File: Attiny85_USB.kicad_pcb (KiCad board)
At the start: 2 copper layers, 40.1 x 12.4 mm, 12 parts, among them J1 Conn_01x04, J2 Conn_01x04, U1 ATtiny85-20M

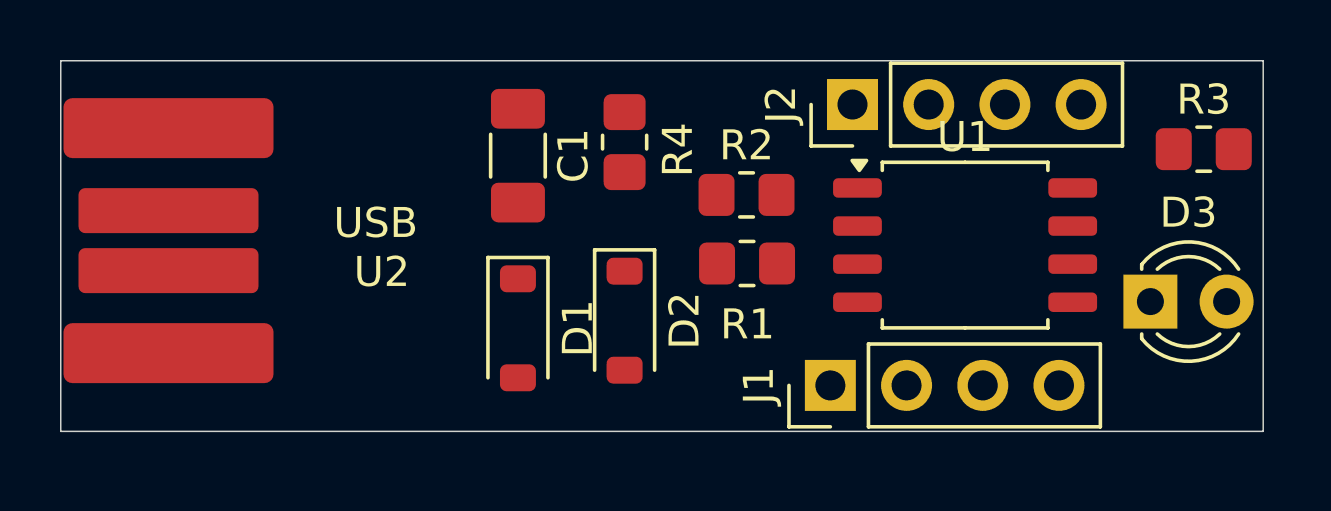
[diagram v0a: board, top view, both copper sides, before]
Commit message: fixing some bugs on the printfoot of the ATtiny85
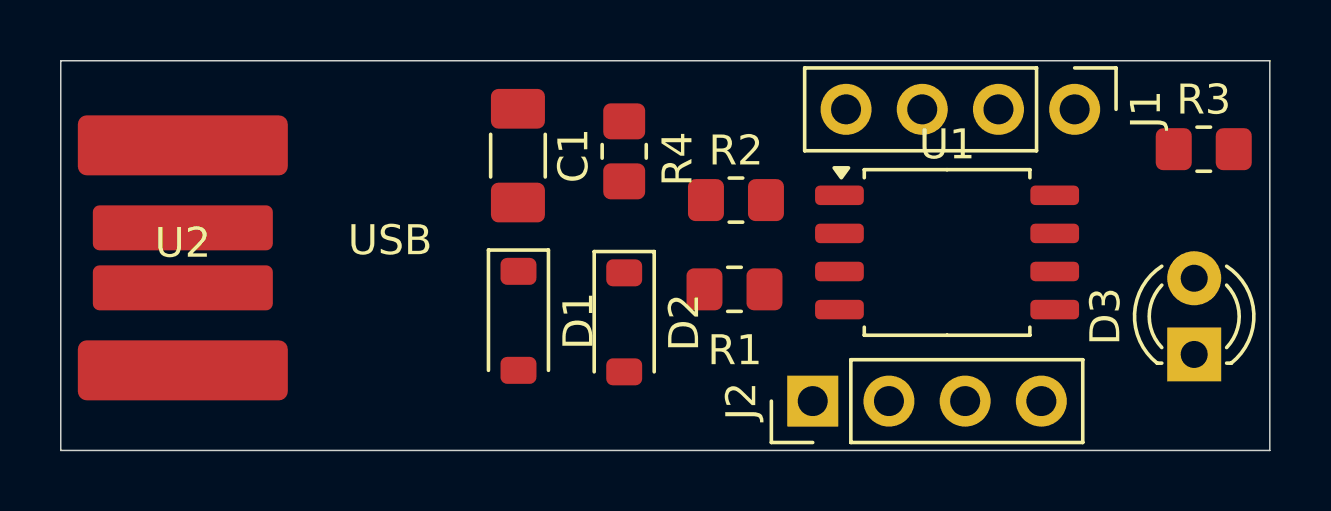
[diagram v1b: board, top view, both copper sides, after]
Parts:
- moved J1 12.3 mm to (139.7, 102.0), turned to -90 degrees
- moved J2 9.97 mm to (131.0, 111.8)
- moved D3 2.29 mm to (143.7, 110.2), turned to 90 degrees
- moved R1 0.96 mm to (128.4, 108.0)
- moved U2 0.75 mm to (110.0, 107.0)
- moved U1 0.65 mm to (135.5, 106.8)
- moved R2 0.39 mm to (128.4, 105.1)
- moved R4 0.31 mm to (124.7, 103.5)
- moved D1 0.25 mm to (121.2, 109.1)
- moved D2 0.06 mm to (124.7, 109.2)
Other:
- board size 40.1 x 12.4 mm -> 40.3 x 13 mm

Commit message: last commit
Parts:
- removed U1: ATtiny85-20M, Package_SO:SOIC-8_5.3x5.3mm_P1.27mm
- added U3: ATtiny85-20S, Package_SO:SOIC-8_5.3x5.3mm_P1.27mm, F.Cu at (135.4, 107.0)
- moved J2 1.07 mm to (132.1, 111.7)
- moved R1 0.58 mm to (128.4, 107.5), turned to 180 degrees
- moved R4 0.48 mm to (124.8, 103.0), turned to -90 degrees
- moved U2 0.40 mm to (109.6, 106.9)
- moved J1 0.25 mm to (139.7, 102.3)
- turned R2 to 180 degrees
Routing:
- net +5V: track 0.00 -> 46.1 mm, vias 0 -> 2
- net GND: track 0.00 -> 37.5 mm
- net Net-(D2-K): track 0.00 -> 23.4 mm
- net Net-(D1-K): track 0.00 -> 19.9 mm, vias 0 -> 1
- net Net-(J2-Pin_3): track 0.00 -> 11.6 mm, vias 0 -> 2
- net Net-(J2-Pin_2): track 0.00 -> 11.0 mm, vias 0 -> 2
- net Net-(J2-Pin_1): track 0.00 -> 8.78 mm, vias 0 -> 2
- net Net-(J1-Pin_3): track 0.00 -> 7.80 mm
- net Net-(J1-Pin_2): track 0.00 -> 7.02 mm
- net Net-(D3-A): track 0.00 -> 4.85 mm
